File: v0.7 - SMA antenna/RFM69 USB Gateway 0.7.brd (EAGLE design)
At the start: 51.3 x 17.2 mm, 26 parts, among them CN1 MINIB, IC3 MCP1703CB, U1 FT231XS, X1 16 MHz

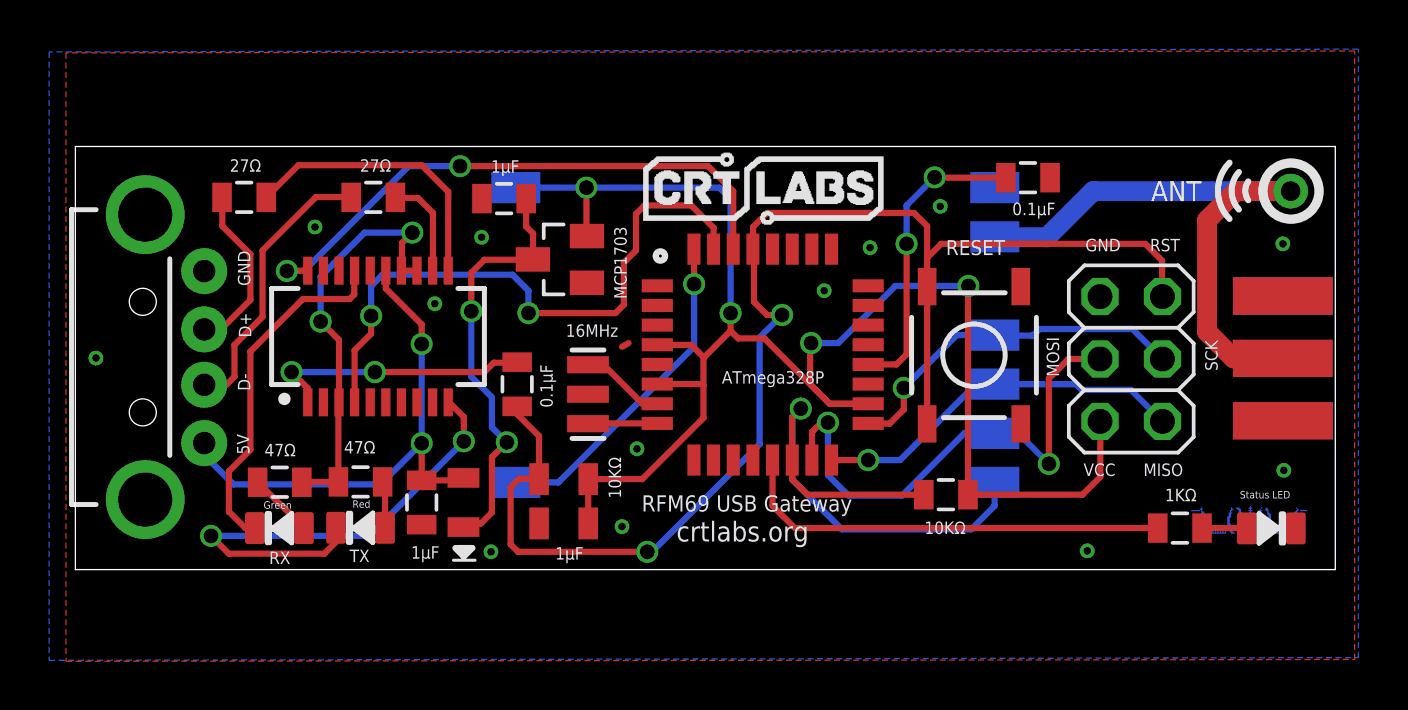
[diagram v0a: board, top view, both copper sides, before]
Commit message: Rounded corners of board
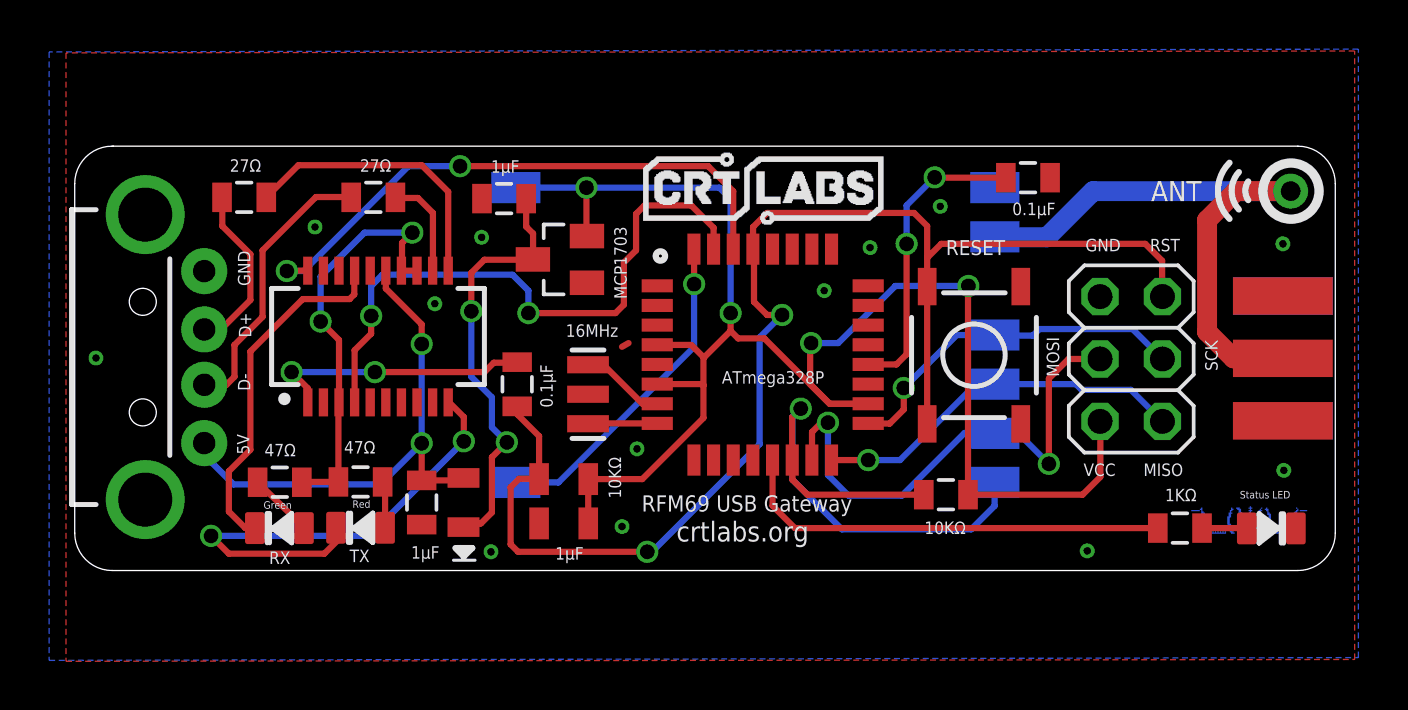
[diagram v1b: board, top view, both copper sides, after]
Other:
- board size 51.3 x 17.2 mm -> 51.3 x 17.3 mm
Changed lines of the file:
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@@
 <rectangle x1="38.42385" y1="19.83105" x2="38.84295" y2="19.86915" layer="121"/>
 <rectangle x1="38.50005" y1="19.86915" x2="38.76675" y2="19.90725" layer="121"/>
-<wire x1="12.1158" y1="20.1549" x2="63.3984" y2="20.1549" width="0" layer="20"/>
-<wire x1="63.3984" y1="20.1549" x2="63.3984" y2="2.9337" width="0" layer="20"/>
-<wire x1="63.3984" y1="2.9337" x2="12.1158" y2="2.9337" width="0" layer="20"/>
-<wire x1="12.1158" y1="2.9337" x2="12.1158" y2="20.1549" width="0" layer="20"/>
 <rectangle x1="60.8838" y1="4.3942" x2="61.4934" y2="4.445" layer="16" rot="R180"/>
 <rectangle x1="60.5282" y1="4.3942" x2="60.6298" y2="4.445" layer="16" rot="R180"/>
@@
 <rectangle x1="57.9374" y1="5.4102" x2="57.9882" y2="5.461" layer="16" rot="R180"/>
 <rectangle x1="59.9186" y1="5.461" x2="59.9694" y2="5.5118" layer="16" rot="R180"/>
+<wire x1="13.6652" y1="20.1676" x2="61.8744" y2="20.1676" width="0" layer="20"/>
+<wire x1="61.8744" y1="2.8956" x2="13.6144" y2="2.8956" width="0" layer="20"/>
+<wire x1="12.0904" y1="4.4196" x2="12.0904" y2="18.6436" width="0" layer="20"/>
+<wire x1="63.3984" y1="4.4196" x2="63.3984" y2="18.6436" width="0" layer="20"/>
+<wire x1="12.0904" y1="18.6436" x2="13.6144" y2="20.1676" width="0" layer="20" curve="-90"/>
+<wire x1="13.6144" y1="20.1676" x2="13.6652" y2="20.1676" width="0" layer="20"/>
+<wire x1="13.6144" y1="2.8956" x2="12.0904" y2="4.4196" width="0" layer="20" curve="-90"/>
+<wire x1="63.3984" y1="4.4196" x2="61.8744" y2="2.8956" width="0" layer="20" curve="-90"/>
+<wire x1="61.8744" y1="20.1676" x2="63.3984" y2="18.6436" width="0" layer="20" curve="-90"/>
 </plain>
 <attributes>
